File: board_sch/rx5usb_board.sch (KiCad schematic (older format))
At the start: 13 parts, among them P1 RX5_WDC, SW1 SWITCH_INV, U1 TEENSYPP2, U2 39SF040

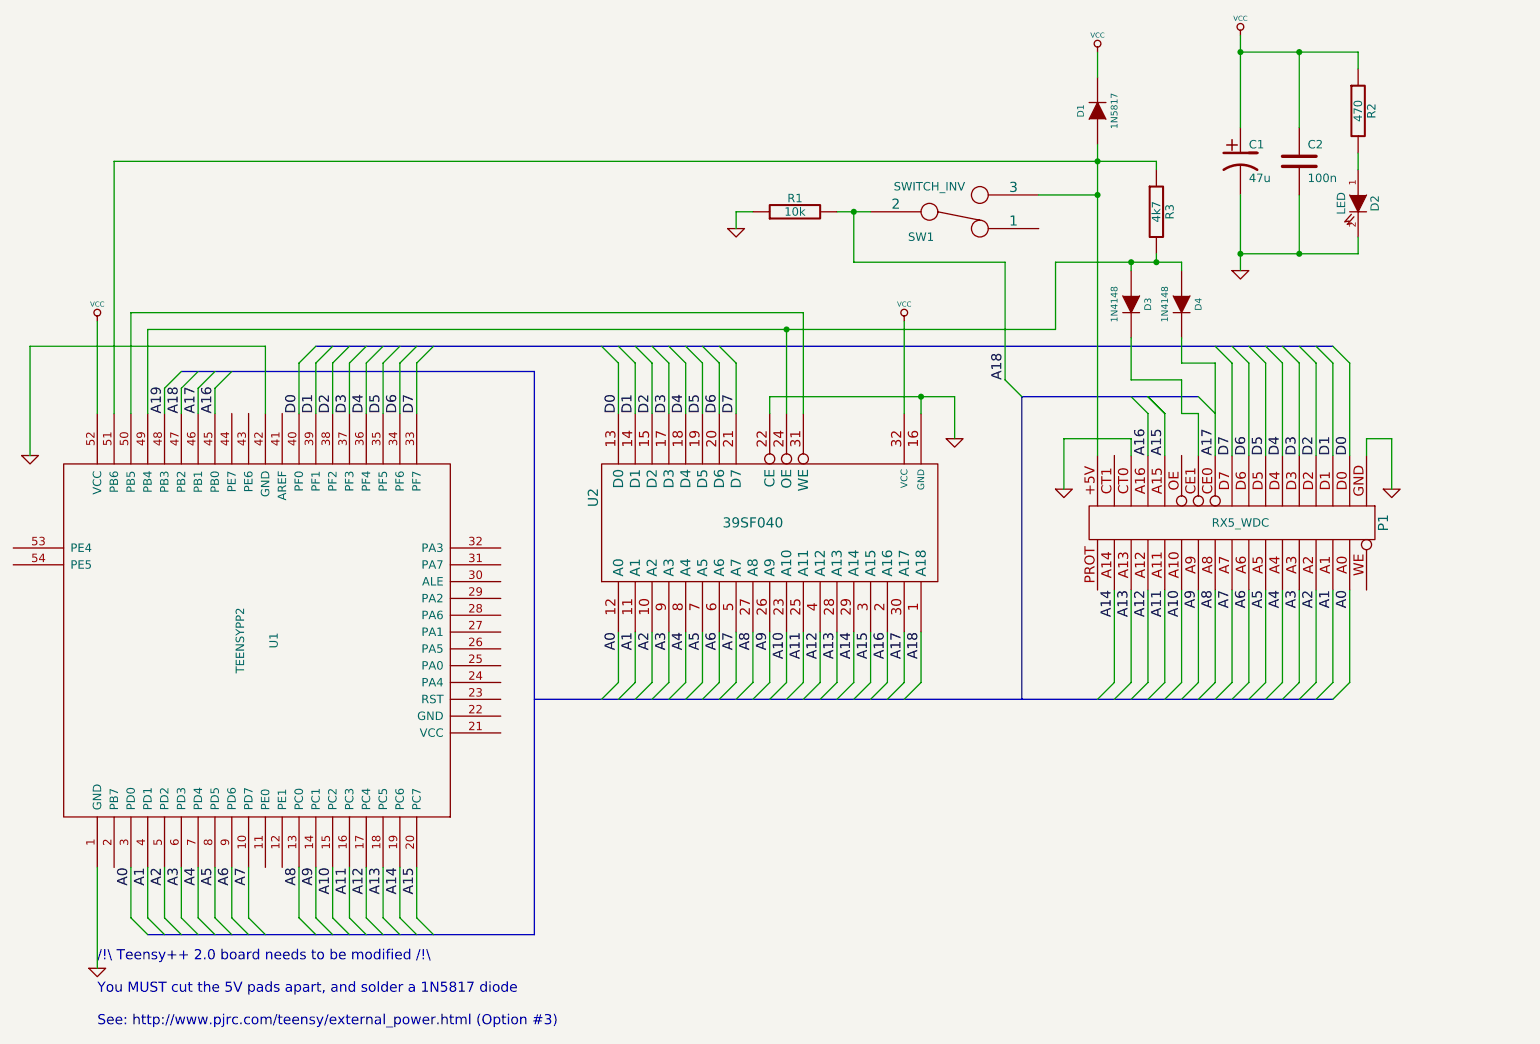
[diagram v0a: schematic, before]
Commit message: board_sch: diode-resistor logic sucks... / more uniform res values
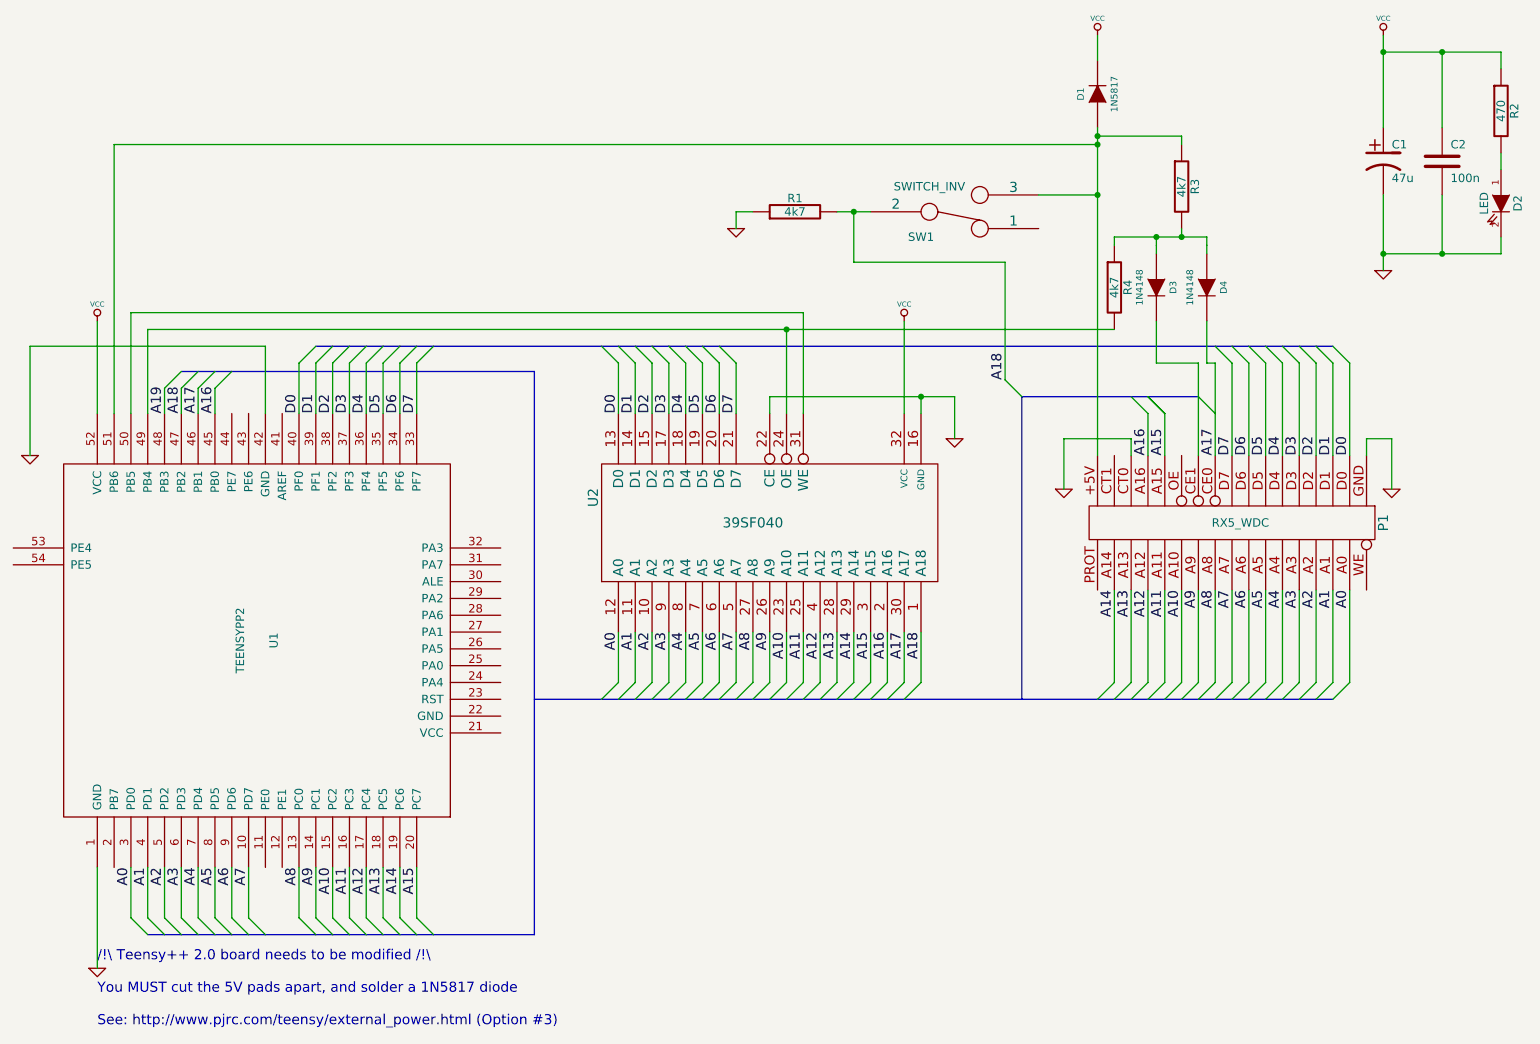
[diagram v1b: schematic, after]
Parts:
- added R4: 4k7, symbol R
- R1: value 10k -> 4k7
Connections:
- net at D3.1 (A), D4.1 (A), R3.2: now also R4.1; no longer U1.49 (PB4), U2.24 (OE)
- new net: R4.2, U1.49 (PB4), U2.24 (OE)
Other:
- moved on the sheet: C1, C2, D1, D2, D3, D4, R2, R3

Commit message: Converted files to modern KiCad format
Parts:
- C1: symbol CP1 -> rx5usb_symbols:CP1
- C2: symbol C -> rx5usb_symbols:C
- D1, D3, D4: symbol DIODE -> rx5usb_symbols:DIODE
- D2: symbol LED -> rx5usb_symbols:LED
- P1: symbol RX5_WDC -> rx5usb_symbols:RX5_WDC
- R1, R2, R3, R4: symbol R -> rx5usb_symbols:R
- SW1: symbol SWITCH_INV -> rx5usb_symbols:SWITCH_INV
- U1: symbol TEENSYPP2 -> rx5usb_symbols:TEENSYPP2
- U2: symbol 39SF040 -> rx5usb_symbols:39SF040

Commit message: Fixed footprint associations
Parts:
- C1: footprint (none) -> rx5usb:C2V8
- C2: footprint (none) -> rx5usb:C2
- D1: footprint (none) -> rx5usb:1N5817
- D3, D4: footprint (none) -> rx5usb:1N4148
- P1: footprint (none) -> rx5usb:RX5_WDC_CART
- R1, R2, R3, R4: footprint (none) -> rx5usb:RESISTOR
- SW1: footprint (none) -> rx5usb:SPTD-3
- U1: footprint MODULE -> rx5usb:TEENSYPP2
- U2: footprint (none) -> rx5usb:U2
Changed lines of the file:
@@
 F 0 "R4" V 8480 2550 50  0000 C CNN
 F 1 "4k7" V 8400 2550 50  0000 C CNN
-F 2 "" H 8400 2550 50  0001 C CNN
+F 2 "rx5usb:RESISTOR" H 8400 2550 50  0001 C CNN
 F 3 "" H 8400 2550 50  0001 C CNN
 	1    8400 2550
@@
 F 0 "D4" H 8950 2650 40  0000 C CNN
 F 1 "1N4148" H 8950 2450 40  0000 C CNN
-F 2 "" H 8950 2550 50  0001 C CNN
+F 2 "rx5usb:1N4148" H 8950 2550 50  0001 C CNN
 F 3 "" H 8950 2550 50  0001 C CNN
 	1    8950 2550
@@
 F 0 "R3" V 8880 1950 50  0000 C CNN
 F 1 "4k7" V 8800 1950 50  0000 C CNN
-F 2 "" H 8800 1950 50  0001 C CNN
+F 2 "rx5usb:RESISTOR" H 8800 1950 50  0001 C CNN
 F 3 "" H 8800 1950 50  0001 C CNN
 	1    8800 1950
@@
 F 0 "D3" H 8650 2650 40  0000 C CNN
 F 1 "1N4148" H 8650 2450 40  0000 C CNN
-F 2 "" H 8650 2550 50  0001 C CNN
+F 2 "rx5usb:1N4148" H 8650 2550 50  0001 C CNN
 F 3 "" H 8650 2550 50  0001 C CNN
 	1    8650 2550
@@
 F 0 "R2" V 10780 1500 50  0000 C CNN
 F 1 "470" V 10700 1500 50  0000 C CNN
-F 2 "" H 10700 1500 50  0001 C CNN
+F 2 "rx5usb:RESISTOR" H 10700 1500 50  0001 C CNN
 F 3 "" H 10700 1500 50  0001 C CNN
 	1    10700 1500
@@
 F 0 "C1" H 10050 1900 50  0000 L CNN
 F 1 "47u" H 10050 1700 50  0000 L CNN
-F 2 "" H 10000 1800 50  0001 C CNN
+F 2 "rx5usb:C2V8" H 10000 1800 50  0001 C CNN
 F 3 "" H 10000 1800 50  0001 C CNN
 	1    10000 1800
@@
 F 0 "C2" H 10400 1900 50  0000 L CNN
 F 1 "100n" H 10400 1700 50  0000 L CNN
-F 2 "" H 10350 1800 50  0001 C CNN
+F 2 "rx5usb:C2" H 10350 1800 50  0001 C CNN
 F 3 "" H 10350 1800 50  0001 C CNN
 	1    10350 1800
@@
 F 0 "R1" V 6580 2100 50  0000 C CNN
 F 1 "4k7" V 6500 2100 50  0000 C CNN
-F 2 "" H 6500 2100 50  0001 C CNN
+F 2 "rx5usb:RESISTOR" H 6500 2100 50  0001 C CNN
 F 3 "" H 6500 2100 50  0001 C CNN
 	1    6500 2100
@@
 F 0 "D1" H 8300 1500 40  0000 C CNN
 F 1 "1N5817" H 8300 1300 40  0000 C CNN
-F 2 "" H 8300 1400 50  0001 C CNN
+F 2 "rx5usb:1N5817" H 8300 1400 50  0001 C CNN
 F 3 "" H 8300 1400 50  0001 C CNN
 	1    8300 1400
@@
 F 0 "SW1" H 7250 2250 50  0000 C CNN
 F 1 "SWITCH_INV" H 7300 1950 50  0000 C CNN
-F 2 "" H 7450 2100 50  0001 C CNN
+F 2 "rx5usb:SPTD-3" H 7450 2100 50  0001 C CNN
 F 3 "" H 7450 2100 50  0001 C CNN
 	1    7450 2100
@@
 F 0 "P1" H 9150 4800 60  0000 C CNN
 F 1 "RX5_WDC" V 9150 3950 50  0000 C CNN
-F 2 "" H 9150 3950 50  0001 C CNN
+F 2 "rx5usb:RX5_WDC_CART" H 9150 3950 50  0001 C CNN
 F 3 "" H 9150 3950 50  0001 C CNN
 	1    9150 3950
@@
 F 0 "U2" H 6400 4900 60  0000 C CNN
 F 1 "39SF040" V 6250 3950 60  0000 C CNN
-F 2 "" H 6250 3950 50  0001 C CNN
+F 2 "rx5usb:U2" H 6250 3950 50  0001 C CNN
 F 3 "" H 6250 3950 50  0001 C CNN
 	1    6250 3950
@@
 F 0 "U1" H 3300 4550 50  0000 C CNN
 F 1 "TEENSYPP2" H 3300 4750 50  0000 C CNN
-F 2 "MODULE" H 3300 4650 50  0001 C CNN
+F 2 "rx5usb:TEENSYPP2" H 3300 4650 50  0001 C CNN
 F 3 "DOCUMENTATION" H 3300 4650 50  0001 C CNN
 	1    3300 4650
@@
 	8650 2250 8650 2350
 Wire Wire Line
+	9000 3000 9000 3550
+Wire Wire Line
 	8900 3000 8900 3550
-Wire Wire Line
-	9000 3000 9000 3550
 Wire Bus Line
 	7850 3200 8900 3200
